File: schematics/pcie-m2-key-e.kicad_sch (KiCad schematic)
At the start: 15 parts, among them J10 Bus_M.2_2199119-6

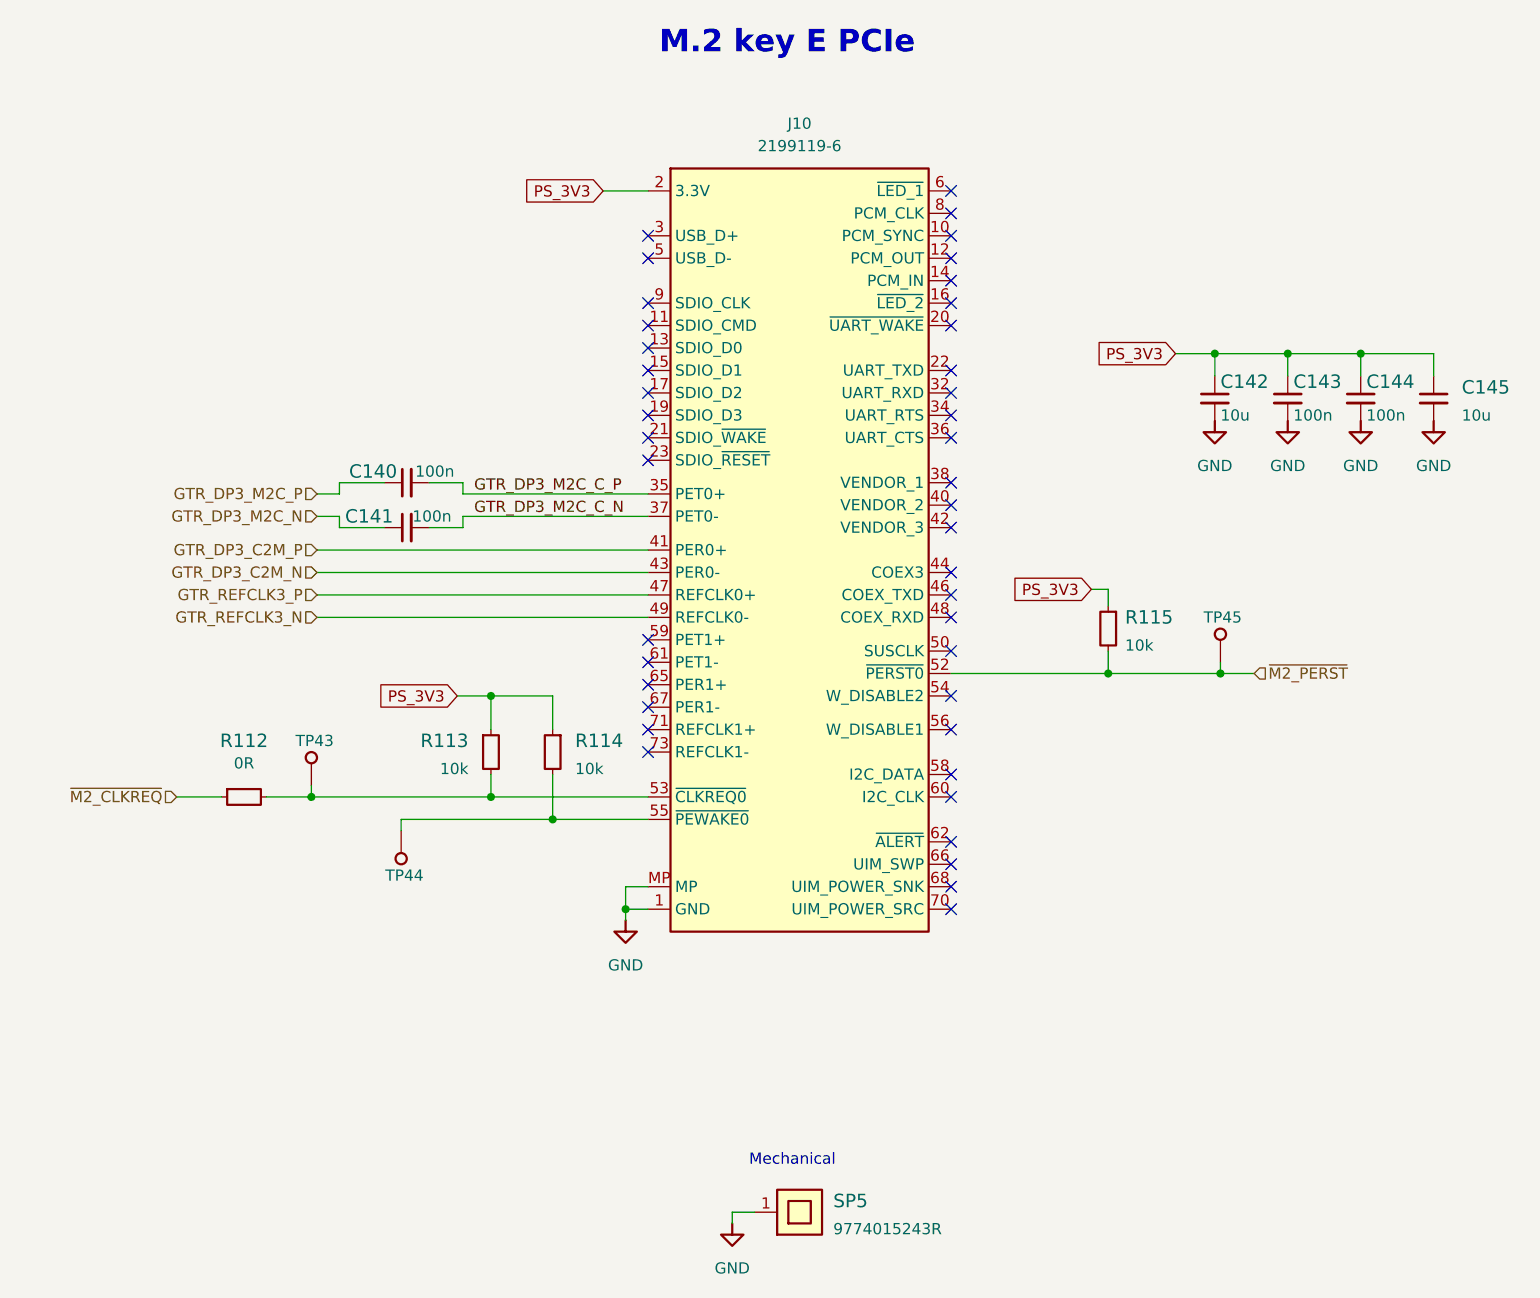
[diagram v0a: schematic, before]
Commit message: Voltage converter added
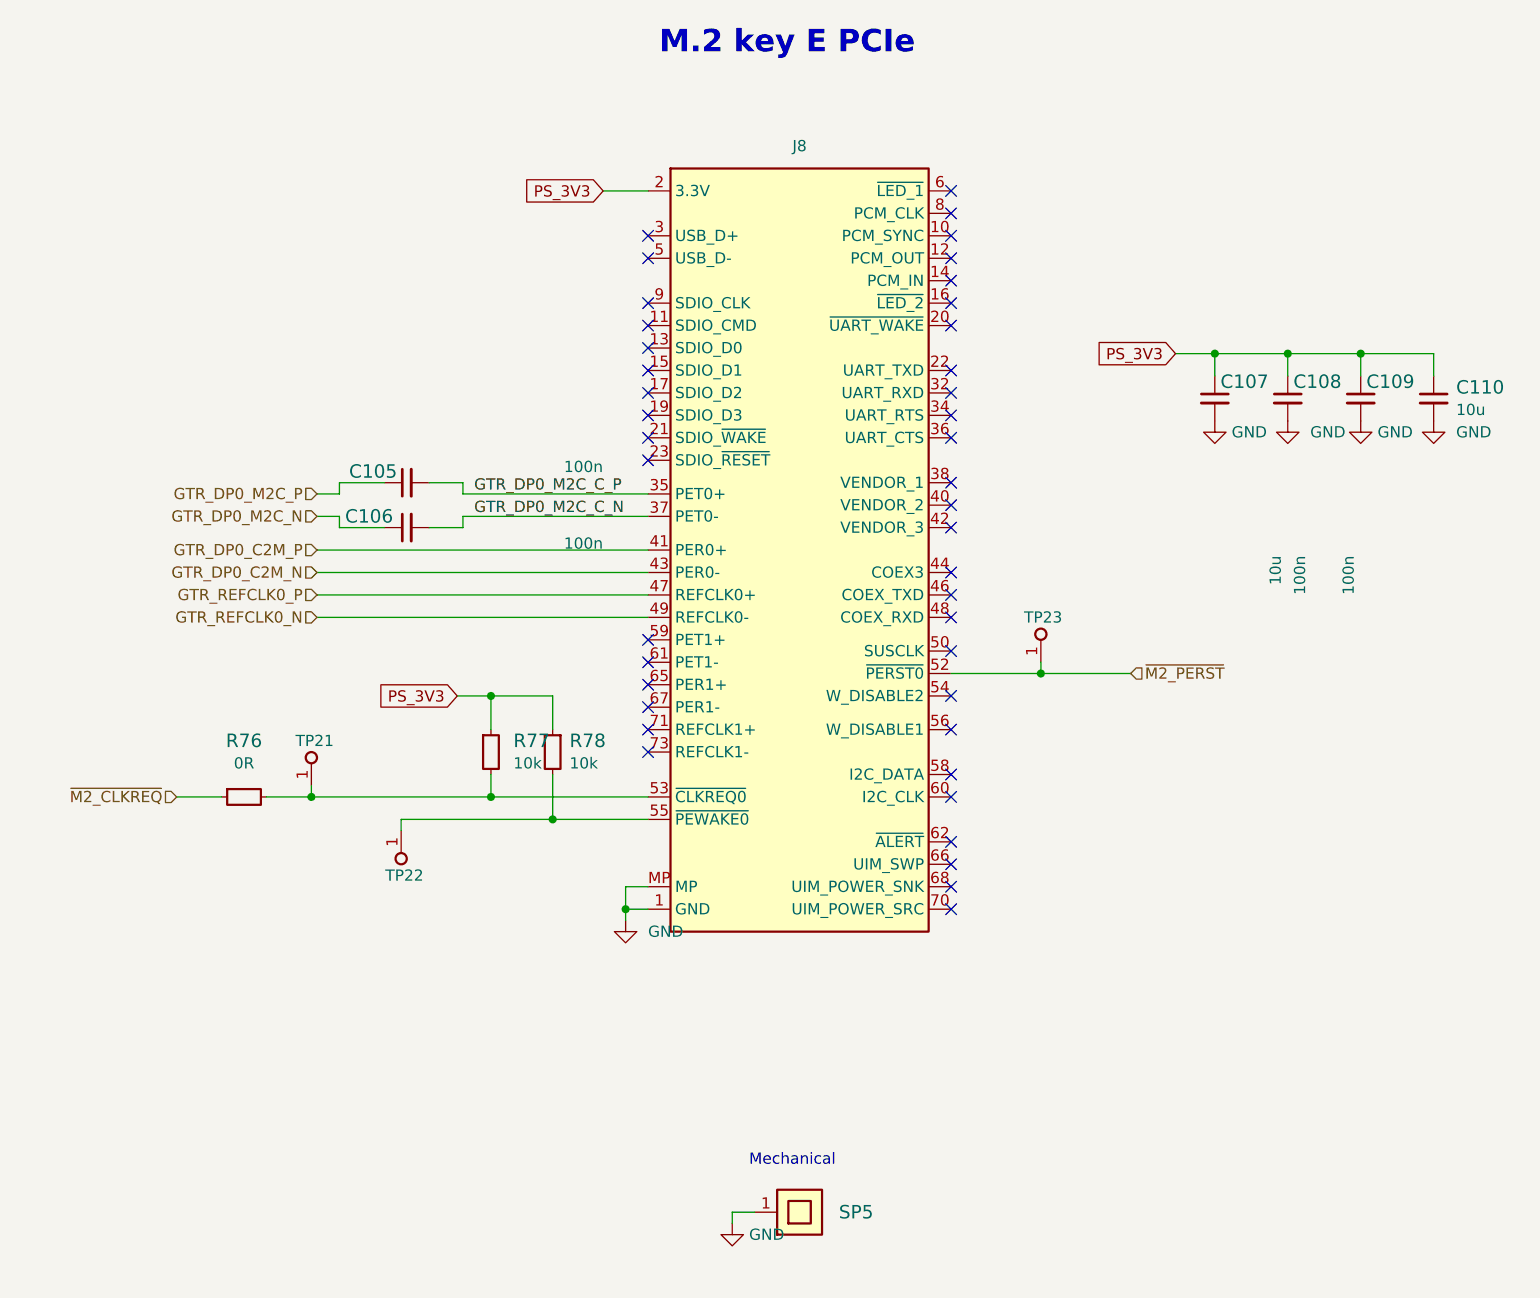
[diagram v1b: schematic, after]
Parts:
- removed R115: R_10k_0402, kria-k26-devboard-footprints:R_0402_1005Metric, symbol kria-k26-devboard:R_10k_0402
- C107: renamed from C142; Dielectric (none) -> template_dielectric
- C110: renamed from C145; Dielectric (none) -> template_dielectric
- J8: renamed from J10; value Bus_M.2_2199119-6 -> Bus_M.2_MDT320E03001
- TP21: renamed from TP43; now left out of the parts list
- TP22: renamed from TP44; now left out of the parts list
- TP23: renamed from TP45; now left out of the parts list
- renumbered C140 to C105, C141 to C106, C143 to C108, C144 to C109, R112 to R76, R113 to R77, R114 to R78
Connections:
- net GTR_DP3_C2M_N renamed GTR_DP0_C2M_N
- net GTR_DP3_C2M_P renamed GTR_DP0_C2M_P
- net GTR_DP3_M2C_C_N renamed GTR_DP0_M2C_C_N
- net GTR_DP3_M2C_C_P renamed GTR_DP0_M2C_C_P
- net GTR_DP3_M2C_N renamed GTR_DP0_M2C_N
- net GTR_DP3_M2C_P renamed GTR_DP0_M2C_P
- net GTR_REFCLK3_N renamed GTR_REFCLK0_N
- net GTR_REFCLK3_P renamed GTR_REFCLK0_P
